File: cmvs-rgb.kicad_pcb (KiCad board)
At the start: 2 copper layers, 69.9 x 39.4 mm, 32 parts, among them U1 THS7374

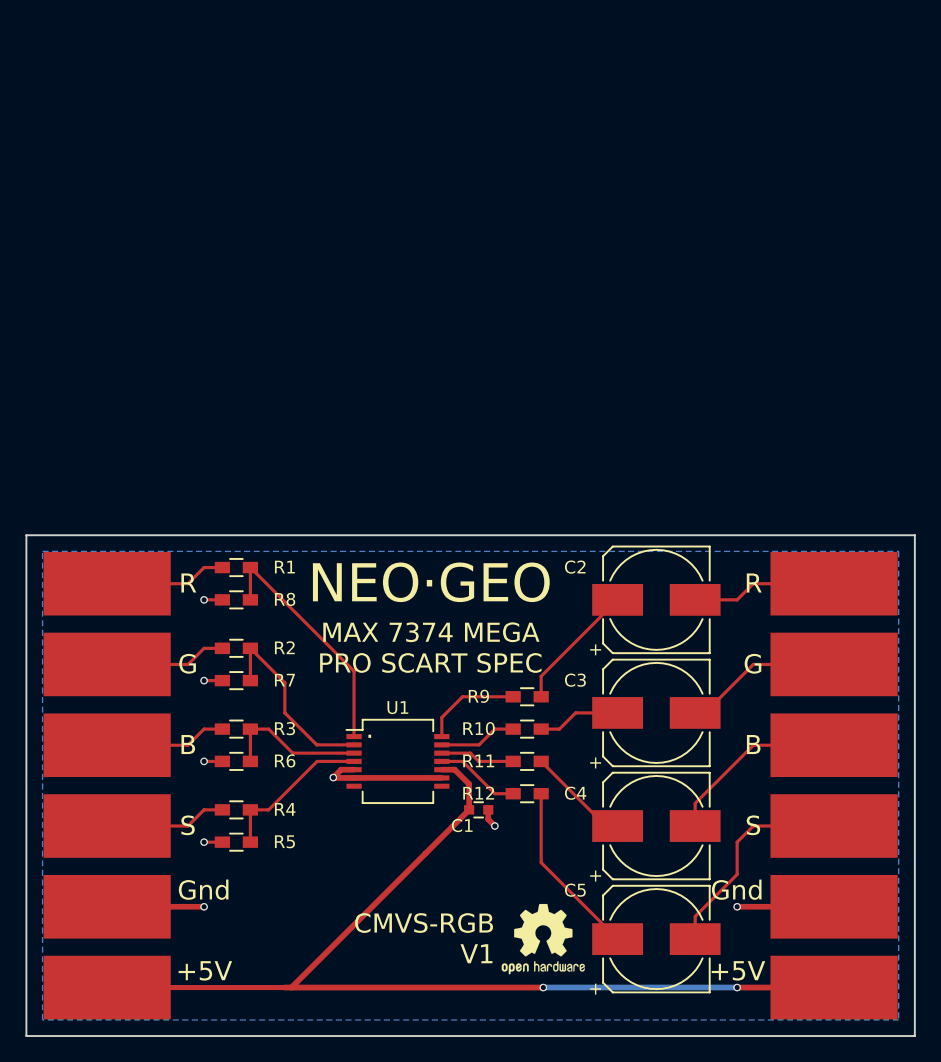
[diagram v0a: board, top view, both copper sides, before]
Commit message: V2
* Footprints changed to 0805 for easier soldering
* Solder pads for enabling/disabling LPF
* Corrected voltage divider for Sync signal, Sync toned down to 0.3V
instead of 0.7V
* Smaller PCB
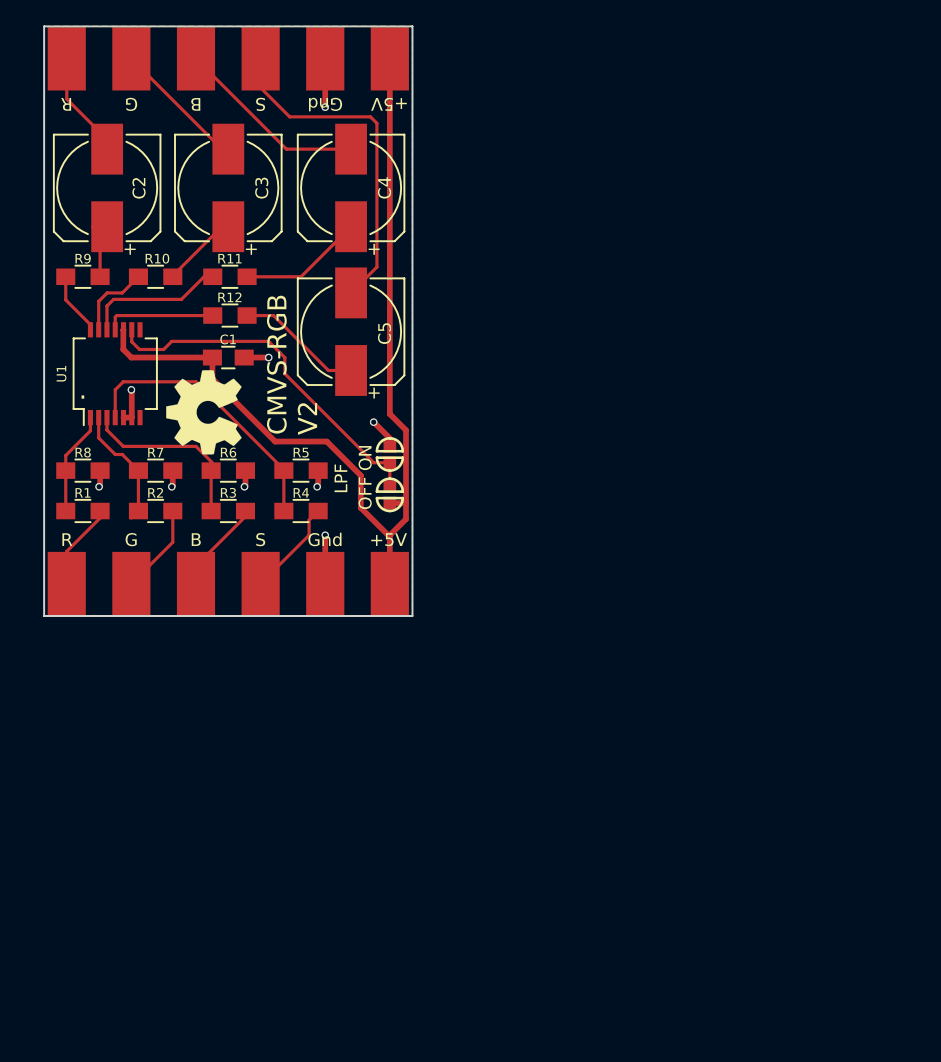
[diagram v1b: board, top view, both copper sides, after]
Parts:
- removed the REF*** at (158.8, 124.5)
- added P1: CONN_01X02, Solderpads:SOLDER-JUMPER_1-WAY, F.Cu at (146.7, 89.5)
- added P2: CONN_01X02, Solderpads:SOLDER-JUMPER_1-WAY, F.Cu at (146.7, 86.4)
- added REF***: OSHW-Symbol_6.7x6mm_SilkScreen, Symbols:OSHW-Symbol_6.7x6mm_SilkScreen, F.Cu at (132.1, 83.1)
- C1: footprint Capacitors_SMD:C_0603 -> Capacitors_SMD:C_0805_HandSoldering
- R1, R10, R11, R12, R2, R3, R4, R6, R7, R8, R9: footprint Resistors_SMD:R_0603_HandSoldering -> Resistors_SMD:R_0805_HandSoldering
- R5: value 1k1 -> 430; footprint Resistors_SMD:R_0603_HandSoldering -> Resistors_SMD:R_0805_HandSoldering
- W1, W10, W11, W12, W2, W3, W4, W5, W6, W7, W8, W9: footprint Wire_Pads:SolderWirePad_single_SMD_5x10mm -> Solderpads:SolderWirePad_single_SMD_3x5mm
- moved W12 80.9 mm to (146.7, 55.2), turned to 0 degrees
- moved W10 77.8 mm to (141.6, 55.2), turned to 0 degrees
- moved W8 75.3 mm to (136.5, 55.2), turned to 0 degrees
- moved W7 73.7 mm to (131.4, 55.2), turned to 0 degrees
- moved W5 73.1 mm to (121.3, 55.2), turned to 0 degrees
- moved W6 72.9 mm to (126.4, 55.2), turned to 0 degrees
- moved G*** 62.5 mm to (141.0, 64.1), turned to 270 degrees
- moved C4 55.6 mm to (143.6, 65.4), turned to 90 degrees
- moved C2 54.0 mm to (124.5, 65.4), turned to 90 degrees
- moved C5 53.4 mm to (143.6, 76.7), turned to 90 degrees
- moved C3 53.3 mm to (134.0, 65.4), turned to 90 degrees
- moved R9 48.1 mm to (122.6, 72.4)
- moved R10 46.0 mm to (128.3, 72.4)
- moved R11 44.7 mm to (134.1, 72.4)
- moved R12 44.3 mm to (134.1, 75.4)
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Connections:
- R2 pad 2: Jamma_Blue -> Jamma_Green
- R3 pad 2: Jamma_Green -> Jamma_Blue
- U1 pad 7: Net-(U1-Pad7) -> (no net)
- U1 pad 8: Net-(U1-Pad8) -> (no net)
- U1 pad 9: GND -> Net-(P1-Pad2)
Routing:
- net Net-(P1-Pad2): track 0.00 -> 28.3 mm
- net GND: track 32.9 -> 20.0 mm, vias 8 -> 9
- net Net-(R1-Pad1): track 19.4 -> 8.26 mm
- net SCART_Sync: track 17.1 -> 27.5 mm
- net Net-(R4-Pad1): track 12.3 -> 21.8 mm
- net +5V: track 82.1 -> 74.7 mm, vias 2 -> 0
- net Net-(R2-Pad1): track 15.4 -> 9.75 mm
- net Net-(R11-Pad2): track 5.88 -> 11.1 mm
- net Net-(C2-Pad1): track 10.1 -> 5.31 mm
- net Net-(C5-Pad1): track 13.9 -> 9.96 mm
- net Net-(R3-Pad1): track 11.5 -> 14.7 mm
- net SCART_Red: track 11.4 -> 8.43 mm
- net Net-(R9-Pad2): track 7.79 -> 4.97 mm
- net Jamma_Red: track 9.59 -> 6.80 mm
- net Jamma_Green: track 9.59 -> 7.06 mm
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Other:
- board size 69.9 x 39.4 mm -> 29 x 46.4 mm
- board text added: "CMVS-RGB V2"
- board text added: "Footprint: SSOP14 0805 0805 0805 0805 0805 8x10"
- board text added: "Jamma Input"
- board text added: "LPF"
- board text added: "OFF"
- board text added: "ON"
- board text added: "Part: U1 R1,R2,R3,R4 R5 R6,R7,R8 R9,R10,R11,R12 C1 C2,C3,C4"
- board text added: "Value: THS7374 6k8 430R 1k4 75R 0.1uF 220uF"
- board text removed: "CMVS-RGB V1"
- board text removed: "Footprint: SSOP14 0603 0603 0603 0603 8x10"
- board text removed: "JAMMA Input"
- board text removed: "MAX 7374 MEGA PRO SCART SPEC"
- board text removed: "NEO⋅GEO"
- board text removed: "Part: U1 R1,R2,R3,R4 R5 R6,R7,R8 C1 C2,C3,C4"
- board text removed: "Value: THS7374 6k8 1k1 1k4 0.1uF 220uF"
